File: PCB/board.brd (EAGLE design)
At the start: 41 x 32 mm, 43 parts, among them J1 USB-A_PTH_MALE, U1 CH340E, U2 NRF52832, Y1 32MHz_2016, Y2 32.768kHz

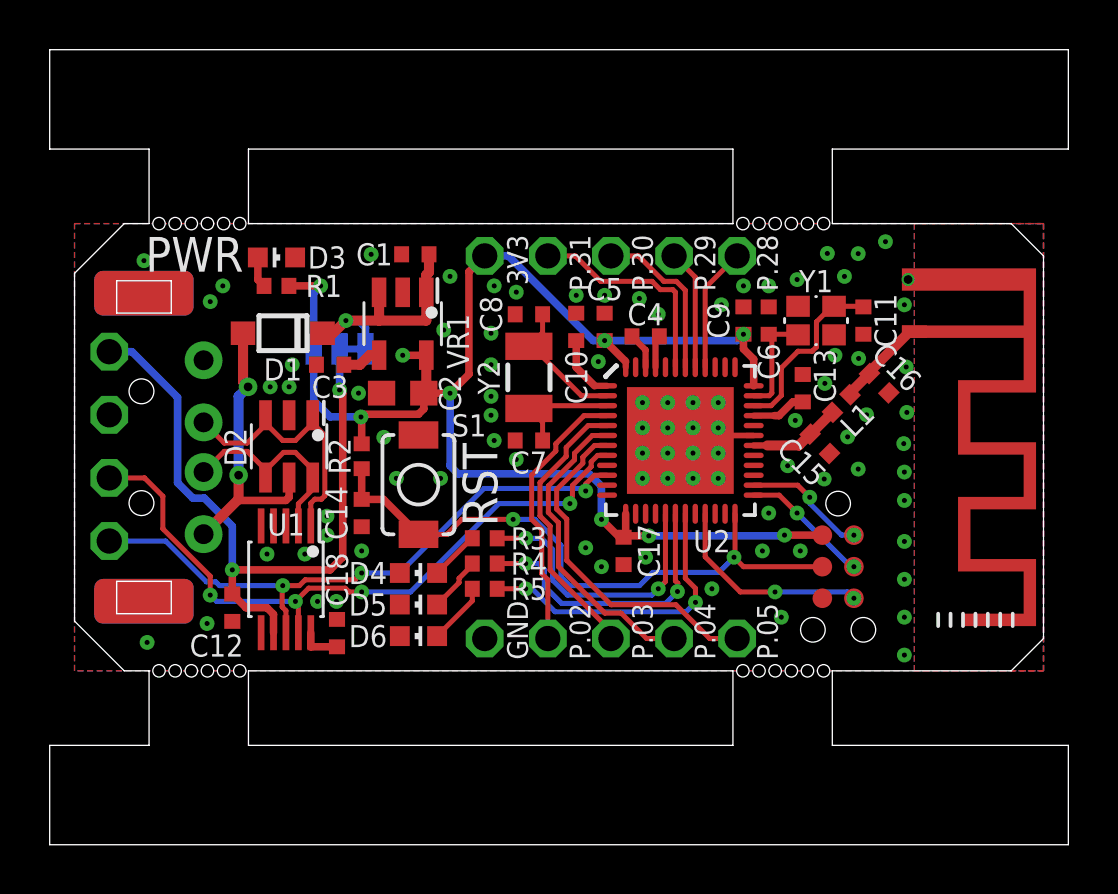
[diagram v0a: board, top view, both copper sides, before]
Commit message: PCB trace width DFM
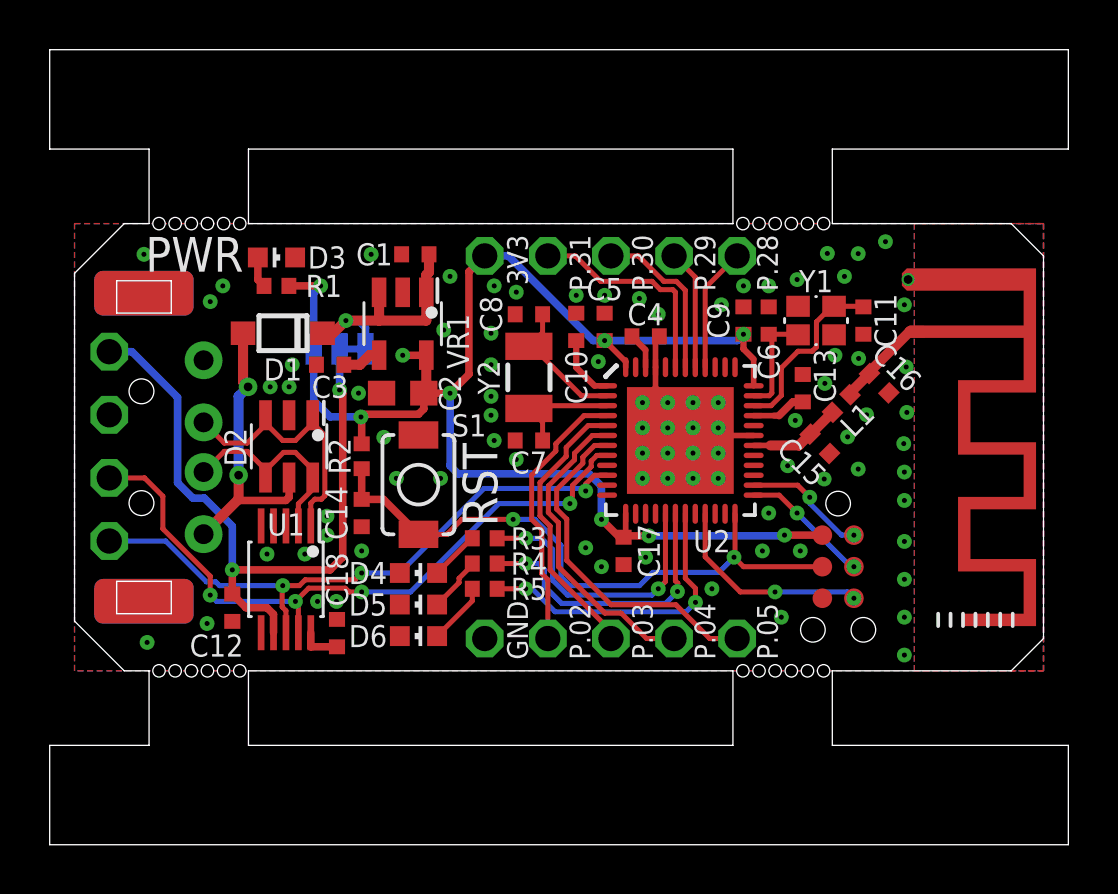
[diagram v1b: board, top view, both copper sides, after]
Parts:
- J1: device angrypig7-Connectors-USB:USB-A-H-RECT -> angrypig7-Connectors-USB:USB-A-MALE-H-PTH-1
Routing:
- net GND: track 2.86 -> 4.49 mm
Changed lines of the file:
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@@
 <drawing>
 <settings>
-<setting alwaysvectorfont="no"/>
+<setting alwaysvectorfont="yes"/>
 <setting verticaltext="up"/>
 </settings>
-<grid distance="10" unitdist="mil" unit="mil" style="lines" multiple="1" display="yes" altdistance="5" altunitdist="mil" altunit="mil"/>
+<grid distance="1" unitdist="mil" unit="mil" style="lines" multiple="1" display="yes" altdistance="5" altunitdist="mil" altunit="mil"/>
 <layers>
 <layer number="1" name="Top" color="4" fill="1" visible="yes" active="yes"/>
@@
 <attribute name="VALUE" x="24.384" y="5.5341" size="1.143" layer="27" font="vector" ratio="12" align="top-center"/>
 </element>
-<element name="J1" library="angrypig7-Connectors-USB" package="USB-A-H-RECT" override_package3d_urn="urn:adsk.eagle:package:25895599/4" override_package_urn="urn:adsk.eagle:footprint:25895600/1" override_locally_modified="yes" value="USB-A_PTH_MALE" x="2.794" y="9" smashed="yes">
+<element name="J1" library="angrypig7-Connectors-USB" package="USB-A-MALE-H-PTH-1" override_package3d_urn="urn:adsk.eagle:package:25895599/4" override_package_urn="urn:adsk.eagle:footprint:25895600/1" override_locally_modified="yes" value="USB-A_PTH_MALE" x="2.794" y="9" smashed="yes">
 <attribute name="LCSC" value="C9739" x="2.794" y="9" size="1.778" layer="27" display="off"/>
 <attribute name="VALUE" x="8.128" y="9.254" size="1.143" layer="27" font="vector" ratio="15" rot="R270" align="bottom-center"/>
@@
 <via x="8.763" y="12.319" extent="1-16" drill="0.2"/>
 <via x="12.446" y="9.398" extent="1-16" drill="0.2"/>
-<wire x1="23.384" y1="12.2216" x2="23.384" y2="13.3082" width="0.254" layer="1"/>
+<wire x1="23.384" y1="12.2216" x2="23.384" y2="13.3082" width="0.2286" layer="1"/>
 <wire x1="23.384" y1="13.3082" x2="23.5378" y2="13.462" width="0.3048" layer="1"/>
 <via x="12.954" y="7.747" extent="1-16" drill="0.2"/>
@@
 <via x="27.686" y="4.826" extent="1-16" drill="0.2"/>
 <via x="32.639" y="17.272" extent="1-16" drill="0.2"/>
-<via x="2.794" y="16.51" extent="1-16" drill="0.2"/>
+<via x="2.794" y="16.764" extent="1-16" drill="0.2"/>
 <via x="5.461" y="14.859" extent="1-16" drill="0.2"/>
 <via x="31.115" y="9.417" extent="1-16" drill="0.2"/>
@@
 <via x="33.4" y="8" extent="1-16" drill="0.2"/>
 <via x="5.334" y="1.905" extent="1-16" drill="0.2"/>
+<wire x1="23.384" y1="12.2216" x2="23.384" y2="11.287" width="0.2286" layer="1"/>
+<wire x1="23.384" y1="11.287" x2="23.876" y2="10.795" width="0.4064" layer="1"/>
 <wire x1="23.876" y1="9.779" x2="24.384" y2="9.271" width="0" layer="19" extent="1-1"/>
 </signal>
@@
 <wire x1="11.557" y1="10.18894375" x2="11.52708125" y2="10.2188625" width="0.3048" layer="1"/>
 <via x="11.52708125" y="10.2188625" extent="1-16" drill="0.2"/>
-<wire x1="27.3346" y1="11.471" x2="27.3346" y2="12.5434" width="0.3048" layer="1"/>
-<wire x1="26.924" y1="12.954" x2="26.924" y2="13.5462" width="0.3048" layer="1"/>
-<wire x1="27.3346" y1="12.5434" x2="26.924" y2="12.954" width="0.3048" layer="1"/>
+<wire x1="27.3346" y1="11.471" x2="27.3346" y2="12.5434" width="0.2286" layer="1"/>
+<wire x1="26.924" y1="12.954" x2="26.924" y2="13.5462" width="0.254" layer="1"/>
+<wire x1="27.3346" y1="12.5434" x2="26.924" y2="12.954" width="0.254" layer="1"/>
 <contactref element="JP3" pad="1"/>
 <wire x1="30.099" y1="5.461" x2="28.575" y2="5.461" width="0.3048" layer="1"/>
@@
 <wire x1="15.875" y1="16.065" x2="15.875" y2="11.938" width="0.3048" layer="1"/>
 <contactref element="JP2" pad="1"/>
-<wire x1="22.184" y1="12.4442" x2="22.184" y2="12.2216" width="0.254" layer="1"/>
-<wire x1="21.336" y1="13.2922" x2="22.184" y2="12.4442" width="0.3048" layer="1"/>
+<wire x1="22.184" y1="12.4442" x2="22.184" y2="12.2216" width="0.2286" layer="1"/>
+<wire x1="21.336" y1="13.2922" x2="22.184" y2="12.4442" width="0.2286" layer="1"/>
 <wire x1="15.44348125" y1="7.92451875" x2="20.71506875" y2="7.92451875" width="0.3048" layer="16"/>
 <wire x1="9.6266" y1="10.8828125" x2="9.6266" y2="12.954" width="0.3048" layer="16"/>
@@
 <wire x1="23.114" y1="5.43108125" x2="22.15228125" y2="5.43108125" width="0.3048" layer="1"/>
 <wire x1="22.15228125" y1="5.43108125" x2="22.098" y2="5.3768" width="0.3048" layer="1"/>
-<wire x1="22.184" y1="6.3204" x2="22.184" y2="5.4628" width="0.3048" layer="1"/>
+<wire x1="22.184" y1="6.3204" x2="22.184" y2="5.4628" width="0.2286" layer="1"/>
 <wire x1="22.184" y1="5.4628" x2="22.098" y2="5.3768" width="0.3048" layer="1"/>
 <wire x1="22.098" y1="5.3768" x2="21.9282" y2="5.3768" width="0.3048" layer="1"/>
@@
 <contactref element="U2" pad="1"/>
 <contactref element="C10" pad="1"/>
-<wire x1="21.4334" y1="11.471" x2="20.93200625" y2="11.471" width="0.254" layer="1"/>
-<wire x1="20.193" y1="12.21000625" x2="20.193" y2="13.2922" width="0.3048" layer="1"/>
-<wire x1="20.93200625" y1="11.471" x2="20.193" y2="12.21000625" width="0.3048" layer="1"/>
+<wire x1="21.4334" y1="11.471" x2="20.93200625" y2="11.471" width="0.2286" layer="1"/>
+<wire x1="20.193" y1="12.21000625" x2="20.193" y2="13.2922" width="0.254" layer="1"/>
+<wire x1="20.93200625" y1="11.471" x2="20.193" y2="12.21000625" width="0.254" layer="1"/>
 </signal>
 <signal name="N$7" class="1">
 <contactref element="U2" pad="46"/>
 <contactref element="C4" pad="1"/>
-<wire x1="22.984" y1="12.2216" x2="22.984" y2="12.9142" width="0.254" layer="1"/>
+<wire x1="22.984" y1="12.2216" x2="22.984" y2="12.9142" width="0.2286" layer="1"/>
 <wire x1="22.984" y1="12.9142" x2="22.4362" y2="13.462" width="0.254" layer="1"/>
 </signal>
@@
 <contactref element="U2" pad="33"/>
 <contactref element="C13" pad="1"/>
-<wire x1="27.3346" y1="10.271" x2="28.1672" y2="10.271" width="0.254" layer="1"/>
-<wire x1="28.1672" y1="10.271" x2="28.3558" y2="10.271" width="0.3048" layer="1"/>
+<wire x1="27.3346" y1="10.271" x2="28.1672" y2="10.271" width="0.2286" layer="1"/>
+<wire x1="28.1672" y1="10.271" x2="28.3558" y2="10.271" width="0.254" layer="1"/>
 <wire x1="28.91" y1="10.8252" x2="28.3558" y2="10.271" width="0.3048" layer="1"/>
 <wire x1="28.91" y1="10.8252" x2="29.31" y2="10.8252" width="0.3048" layer="1"/>
@@
 <wire x1="31.214553125" y1="11.1845" x2="31.995525" y2="11.965471875" width="0.4064" layer="1"/>
 <wire x1="31.995525" y1="12.035525" x2="31.995525" y2="11.965471875" width="0.4064" layer="1"/>
-<wire x1="33.81" y1="13.65" x2="33.61" y2="13.65" width="0.4064" layer="1"/>
+<wire x1="33.91" y1="13.65" x2="33.61" y2="13.65" width="0.4064" layer="1"/>
 <wire x1="33.61" y1="13.65" x2="31.995525" y2="12.035525" width="0.4064" layer="1"/>
 </signal>
@@
 <via x="8.89" y="2.794" extent="1-16" drill="0.2"/>
 <contactref element="U2" pad="8"/>
-<wire x1="8.89" y1="2.794" x2="9.017" y2="2.667" width="0.2032" layer="1"/>
 <wire x1="8.89" y1="2.794" x2="9.42368125" y2="3.32768125" width="0.2032" layer="1"/>
 <wire x1="9.42368125" y1="3.32768125" x2="10.89631875" y2="3.32768125" width="0.2032" layer="1"/>
@@
 <wire x1="19.939" y1="6.731" x2="20.04031875" y2="6.83231875" width="0.2032" layer="1"/>
 <wire x1="20.04031875" y1="7.46008125" x2="20.04031875" y2="6.83231875" width="0.2032" layer="1"/>
-<wire x1="20.79436875" y1="8.21413125" x2="20.79436875" y2="8.41335625" width="0.2032" layer="1"/>
+<wire x1="20.79436875" y1="8.21413125" x2="20.79436875" y2="8.43875625" width="0.2032" layer="1"/>
 <wire x1="20.79436875" y1="8.21413125" x2="20.04031875" y2="7.46008125" width="0.2032" layer="1"/>
-<wire x1="21.0520125" y1="8.671" x2="21.4334" y2="8.671" width="0.2032" layer="1"/>
-<wire x1="20.79436875" y1="8.41335625" x2="21.0520125" y2="8.671" width="0.2032" layer="1"/>
+<wire x1="21.0266125" y1="8.671" x2="21.4334" y2="8.671" width="0.2032" layer="1"/>
+<wire x1="20.79436875" y1="8.43875625" x2="21.0266125" y2="8.671" width="0.2032" layer="1"/>
 <wire x1="5.715" y1="2.794" x2="5.461" y2="3.048" width="0.2032" layer="16"/>
 <via x="5.461" y="3.048" extent="1-16" drill="0.2"/>
@@
 <wire x1="3.556" y1="5.715" x2="3.556" y2="7.0261625" width="0.2032" layer="1"/>
 <contactref element="U1" pad="9"/>
+<wire x1="9.009" y1="2.675" x2="9.009" y2="1.533" width="0.2032" layer="1"/>
 <wire x1="8.89" y1="2.794" x2="9.009" y2="2.675" width="0.2032" layer="1"/>
-<wire x1="9.009" y1="2.675" x2="9.009" y2="1.533" width="0.2032" layer="1"/>
 </signal>
 <signal name="N$6">
@@
 <contactref element="L1" pad="1"/>
 <contactref element="C15" pad="1"/>
-<wire x1="27.3346" y1="9.071" x2="27.886" y2="9.071" width="0.254" layer="1"/>
+<wire x1="27.3346" y1="9.071" x2="28.013" y2="9.071" width="0.2286" layer="1"/>
 <wire x1="29.609525" y1="9.525471875" x2="29.626471875" y2="9.525471875" width="0.4064" layer="1"/>
 <wire x1="30.50744375" y1="10.40644375" x2="29.626471875" y2="9.525471875" width="0.4064" layer="1"/>
 <wire x1="29.155053125" y1="9.071" x2="29.609525" y2="9.525471875" width="0.4064" layer="1"/>
-<wire x1="27.886" y1="9.071" x2="29.155053125" y2="9.071" width="0.4064" layer="1"/>
+<wire x1="28.013" y1="9.071" x2="29.155053125" y2="9.071" width="0.4064" layer="1"/>
 </signal>
 <signal name="GND-CUTOUT">
